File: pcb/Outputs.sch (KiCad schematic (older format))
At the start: 44 parts, among them P66 IG2, P67 IG1, P81 IG3, P82 IG4, P84 Ignitor2, P85 Ignitor1, P86 Ignitor3, P87 Ignitor4, Q10 VNN7NV0413TR, Q11 VNN7NV0413TR, Q9 VNN7NV0413TR, U12 TC442XA, U9 TC442XA

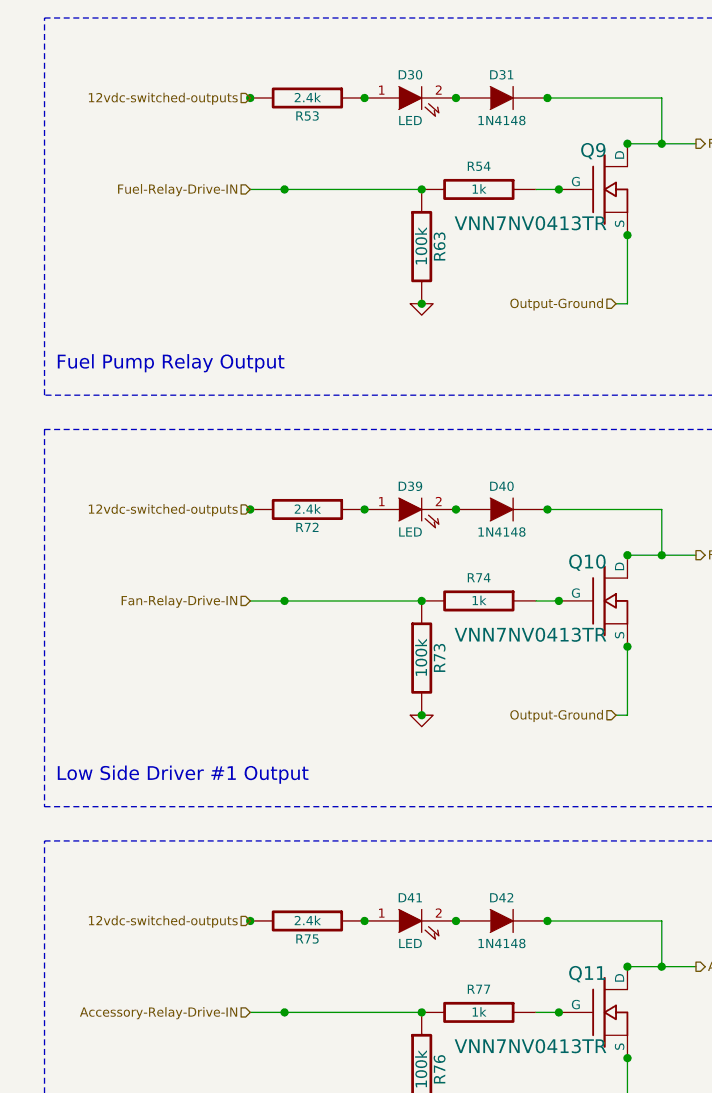
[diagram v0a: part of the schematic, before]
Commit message: Changed 2.4k ohm resistor to 2.43k ohm resistor due to physical size issue.
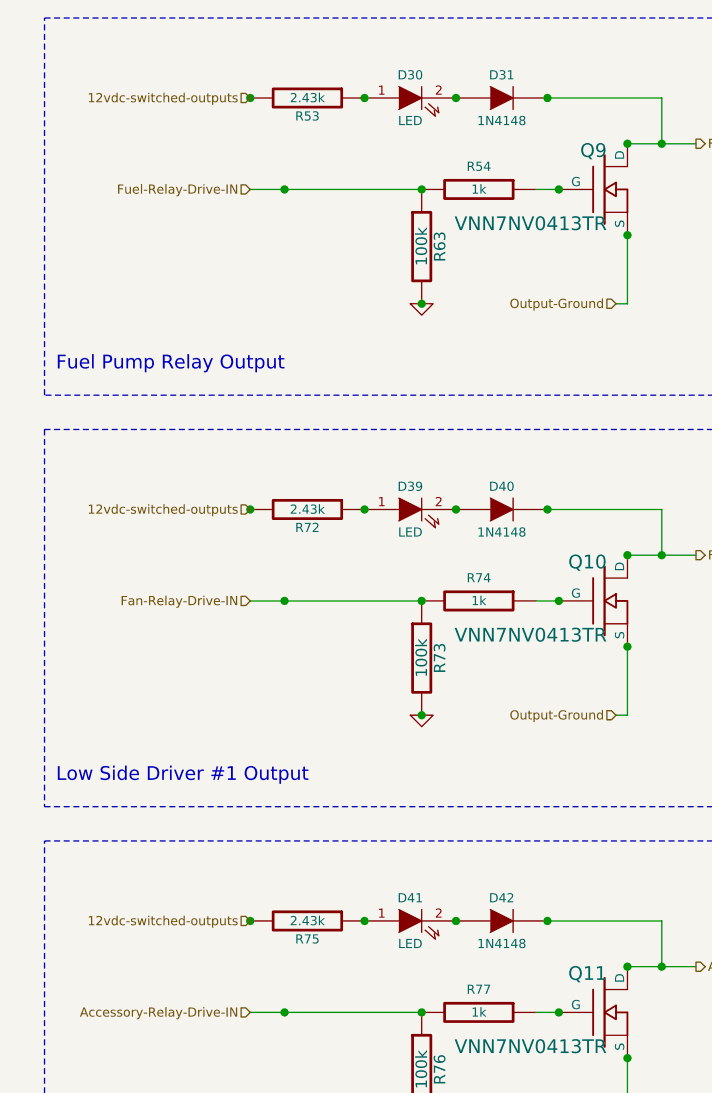
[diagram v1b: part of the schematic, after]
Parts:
- R53, R72, R75: value 2.4k -> 2.43k

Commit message: Added LEDs and resistors to ignitor outputs.
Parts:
- removed D31: 1N4148, symbol DIODE
- removed Q9: VNN7NV0413TR, symbol MOSFET_N
- added D? (x4): LED, symbol LED
- added R?: 1k, symbol R
- added R? (x4): 2.4k, symbol R
- added U?: VN5E160AS-E, symbol VN5E160AS-E
- R?: renamed from R53; value 2.43k -> 2.4k
- R?: renamed from R72; value 2.43k -> 2.4k
- R?: renamed from R75; value 2.43k -> 2.4k
- R?: renamed from R91; value 160 -> 100
- R?: renamed from R92; value 160 -> 100
- R?: renamed from R101; value 160 -> 100
- R?: renamed from R100; value 160 -> 100
- renumbered C52 to C?, C57 to C?, D30 to D?, D40 to D?, D39 to D?, D41 to D?, D42 to D?, JP1 to JP?, JP2 to JP?, P66 to P?, P67 to P?, P82 to P?, P81 to P?, P85 to P?, P84 to P?, P87 to P?, P86 to P?, Q10 to Q?, Q11 to Q?, R54 to R?, R63 to R?, R73 to R?, R74 to R?, R77 to R?, R76 to R?, R90 to R?, R89 to R?, R88 to R?, R87 to R?, R104 to R?, R105 to R?, R102 to R?, R103 to R?, U9 to U?, U12 to U?
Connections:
- net labels added: 5vdc-analog, LSD1-IN, LSD1_Relay, PCB-GND
- net labels removed: 5vdc-cpu, Accessory-Relay-Drive-IN, Accessory_Relay
- wire segments 55 -> 62
- no-connect marks 4 -> 5
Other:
- note added: "Fuel Pump Relay High Side Driver Output"
- note added: "JP11 selects either\n5v or 12v \nDriver IC Supply"
- note added: "JPxx selects either\n5v or 12v \nDriver IC Supply"
- note added: "Radiator Cooling Fan Low Side Driver Output"
- note removed: "Fuel Pump Relay Output"
- note removed: "JP1 selects either\n5v or 12v \nDriver IC Supply"
- note removed: "JP2 selects either\n5v or 12v \nDriver IC Supply"
- note removed: "Low Side Driver #2 Output"
- note removed: "\nTC4426A has two inverting drivers, \nwhile the TC4427A has two non-inverting drivers, \nThe TC4428A has one inverting and one non-inverting driver."
- moved on the sheet: C?, D?, JP?, R?

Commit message: Changed fuel pump LSD out for high side driver, removed Fan and LSD1 individual low side drivers for a pair of dual MOSFET low side drivers.
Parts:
- removed D?: LED, symbol LED
- removed D?: 1N4148, symbol DIODE
- removed Q? (x2): VNN7NV0413TR, symbol MOSFET_N
- removed R?: 1k, symbol R
- removed R?: 2.4k, symbol R
- removed R?: 100k, symbol R
- added D? (x3): LED, symbol LED
- added D? (x3): 1N4148, symbol DIODE
- added R? (x3): 1k, symbol R
- added R? (x3): 100k, symbol R
- added R? (x3): 2.4k, symbol R
- added U?, U??: VNS3NV04D, ~, symbol VNS3NV04D
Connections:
- net labels added: LSD1, LSD2, LSD2-IN, LSD3, LSD3-IN
- net labels removed: LSD1_Relay
- wire segments 62 -> 91
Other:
- moved on the sheet: D?, R?

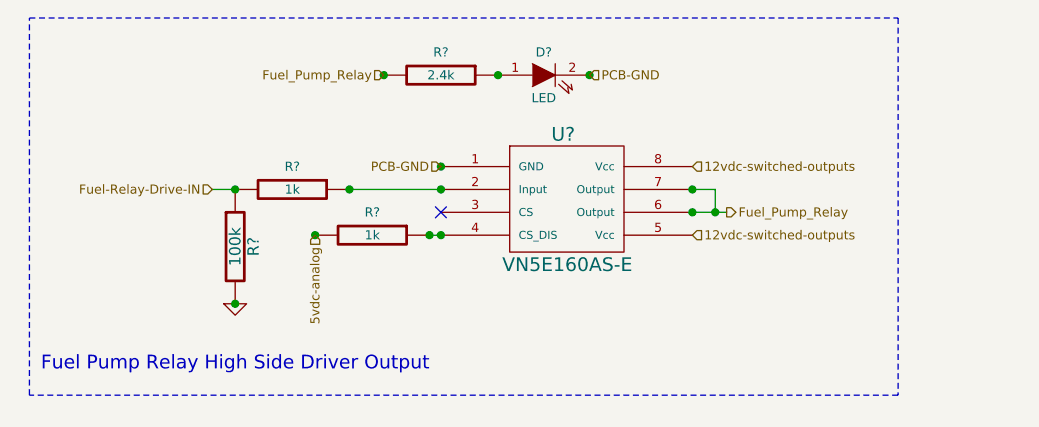
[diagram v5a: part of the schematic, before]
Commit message: Removed direct connection between Port A7 and the Fuel Pump HSD and added connection points to solder a jumper wire to select fuel pump HSD or LSD circuit.
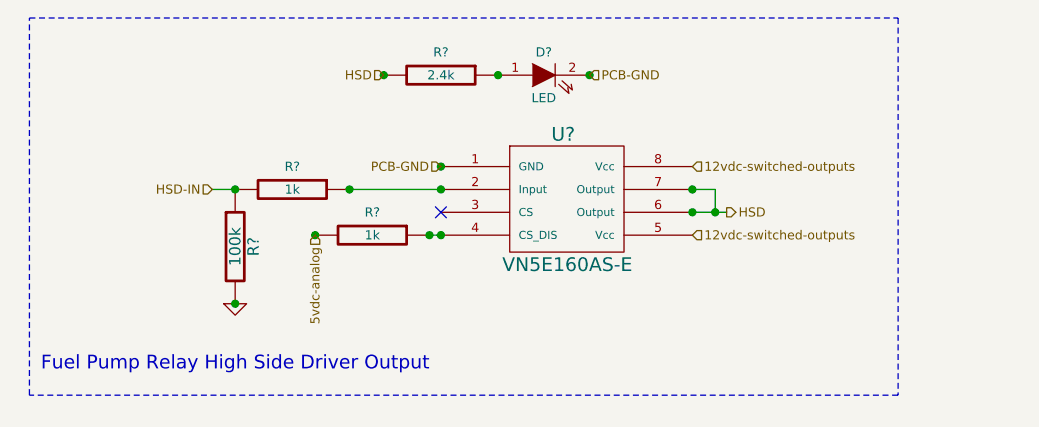
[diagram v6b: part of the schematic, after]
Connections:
- net labels added: HSD, HSD-IN
- net labels removed: Fuel-Relay-Drive-IN, Fuel_Pump_Relay
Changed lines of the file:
@@
 $EndComp
 Text HLabel 1450 1350 0    40   Input ~ 0
-Fuel-Relay-Drive-IN
-Text HLabel 2200 850  0    40   Input ~ 0
-Fuel_Pump_Relay
+HSD-IN
 $Comp
 L R R?
@@
 12vdc-switched-outputs
 Text HLabel 3700 1450 2    40   Output ~ 0
-Fuel_Pump_Relay
+HSD
 Wire Wire Line
 	3550 1450 3650 1450
@@
 	4250 5150 4250 5350
 Connection ~ 4250 5350
+Text HLabel 2200 850  0    40   Input ~ 0
+HSD
 $EndSCHEMATC

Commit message: Changed revision to 0.7-alpha and git hash to xxxxxxxxxx to show that this is in progress.
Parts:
- removed D? (x4): 1N4148, symbol DIODE
- removed D? (x7): LED, symbol LED
- removed R? (x4): 1k, symbol R
- removed R? (x7): 2.4k, symbol R
- removed R? (x3): 100k, symbol R
- removed U?: VN5E160AS-E, symbol VN5E160AS-E
- removed U?, U??: VNS3NV04D, ~, symbol VNS3NV04D
- added D40, D42, D? (x2): 1N4148, symbol DIODE
- added D41, D? (x4): LED, symbol LED
- added R75, R? (x4): 2.4k, symbol R
- added R76, R? (x2): 100k, symbol R
- added R77, R? (x3): 1k, symbol R
- added U??: VN5E160AS-E, ~, symbol VN5E160AS-E
- added U?? (x2): VNS3NV04D, ~, symbol VNS3NV04D
- R100, R101, R91, R92: renamed from R?; value 100 -> 160
- gave numbers to parts that had none: 30
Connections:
- net labels added: 5vdc-cpu, Fan-IN
- net labels removed: 5vdc-analog, Fan-Relay-Drive-IN
- wire segments 91 -> 78
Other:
- note added: "Fuel Pump Relay Output"
- note added: "JP1 selects either\n5v or 12v \nDriver IC Supply"
- note added: "JP2 selects either\n5v or 12v \nDriver IC Supply"
- note added: "Low Side Driver #2 and #3 Outputs"
- note added: "Radiator Fan and Low Side Driver #1 Outputs"
- note added: "\nTC4426A has two inverting drivers, \nwhile the TC4427A has two non-inverting drivers, \nThe TC4428A has one inverting and one non-inverting driver."
- note removed: "Fuel Pump Relay High Side Driver Output"
- note removed: "JP11 selects either\n5v or 12v \nDriver IC Supply"
- note removed: "JPxx selects either\n5v or 12v \nDriver IC Supply"
- note removed: "Low Side Driver #1 Output"
- note removed: "Radiator Cooling Fan Low Side Driver Output"
- moved on the sheet: C52, C57, D30, D39, JP1, JP2, R53, R54, R63, R72, R73, R74

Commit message: Started laying out PCB changes for SO-8 high side driver and new SO-8 low side drivers.
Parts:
- gave numbers to parts that had none: 18
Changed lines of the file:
@@
 Sheet 5 7
 Title "Jaguar PCB for FreeEMS"
-Date "5 feb 2014"
+Date "4 mar 2014"
 Rev "0.7-alpha"
 Comp "Git: xxxxxxxxxx"
@@
 Connection ~ 1200 1850
 Connection ~ 3200 850
-Connection ~ 1550 950
 Connection ~ 3600 850
 Wire Notes Line
@@
 $EndComp
 $Comp
-L GND #PWR029
+L GND #PWR40
 U 1 1 509C8648
 P 7700 4100
-F 0 "#PWR029" H 7700 4100 30  0001 C CNN
+F 0 "#PWR40" H 7700 4100 30  0001 C CNN
 F 1 "GND" H 7700 4030 30  0001 C CNN
 F 2 "" H 7700 4100 60  0001 C CNN
@@
 $EndComp
 $Comp
-L GND #PWR030
+L GND #PWR36
 U 1 1 509C8647
 P 7550 2900
-F 0 "#PWR030" H 7550 2900 30  0001 C CNN
+F 0 "#PWR36" H 7550 2900 30  0001 C CNN
 F 1 "GND" H 7550 2830 30  0001 C CNN
 F 2 "" H 7550 2900 60  0001 C CNN
@@
 $EndComp
 $Comp
-L GND #PWR031
+L GND #PWR39
 U 1 1 509C8646
 P 7700 3450
-F 0 "#PWR031" H 7700 3450 30  0001 C CNN
+F 0 "#PWR39" H 7700 3450 30  0001 C CNN
 F 1 "GND" H 7700 3380 30  0001 C CNN
 F 2 "" H 7700 3450 60  0001 C CNN
@@
 $EndComp
 $Comp
-L GND #PWR032
+L GND #PWR44
 U 1 1 509C8641
 P 9800 3900
-F 0 "#PWR032" H 9800 3900 30  0001 C CNN
+F 0 "#PWR44" H 9800 3900 30  0001 C CNN
 F 1 "GND" H 9800 3830 30  0001 C CNN
 F 2 "" H 9800 3900 60  0001 C CNN
@@
 JP1 selects either\n5v or 12v \nDriver IC Supply
 $Comp
-L GND #PWR033
+L GND #PWR43
 U 1 1 5092C12A
 P 9800 1950
-F 0 "#PWR033" H 9800 1950 30  0001 C CNN
+F 0 "#PWR43" H 9800 1950 30  0001 C CNN
 F 1 "GND" H 9800 1880 30  0001 C CNN
 F 2 "" H 9800 1950 60  0001 C CNN
@@
 $EndComp
 $Comp
-L GND #PWR034
+L GND #PWR37
 U 1 1 5092BF20
 P 7700 1500
-F 0 "#PWR034" H 7700 1500 30  0001 C CNN
+F 0 "#PWR37" H 7700 1500 30  0001 C CNN
 F 1 "GND" H 7700 1430 30  0001 C CNN
 F 2 "" H 7700 1500 60  0001 C CNN
@@
 $EndComp
 $Comp
-L GND #PWR035
+L GND #PWR35
 U 1 1 5092BF13
 P 7550 950
-F 0 "#PWR035" H 7550 950 30  0001 C CNN
+F 0 "#PWR35" H 7550 950 30  0001 C CNN
 F 1 "GND" H 7550 880 30  0001 C CNN
 F 2 "" H 7550 950 60  0001 C CNN
@@
 $EndComp
 $Comp
-L GND #PWR036
+L GND #PWR38
 U 1 1 5092BF09
 P 7700 2150
-F 0 "#PWR036" H 7700 2150 30  0001 C CNN
+F 0 "#PWR38" H 7700 2150 30  0001 C CNN
 F 1 "GND" H 7700 2080 30  0001 C CNN
 F 2 "" H 7700 2150 60  0001 C CNN
@@
 12vdc-switched-outputs
 $Comp
-L GND #PWR037
+L GND #PWR30
 U 1 1 4F2F3E3F
 P 1100 5500
-F 0 "#PWR037" H 1100 5500 30  0001 C CNN
+F 0 "#PWR30" H 1100 5500 30  0001 C CNN
 F 1 "GND" H 1100 5430 30  0001 C CNN
 F 2 "" H 1100 5500 60  0001 C CNN
@@
 $EndComp
 $Comp
-L GND #PWR038
+L GND #PWR29
 U 1 1 4F2F3E2D
 P 1100 3650
-F 0 "#PWR038" H 1100 3650 30  0001 C CNN
+F 0 "#PWR29" H 1100 3650 30  0001 C CNN
 F 1 "GND" H 1100 3580 30  0001 C CNN
 F 2 "" H 1100 3650 60  0001 C CNN
@@
 $EndComp
 $Comp
-L GND #PWR039
+L GND #PWR31
 U 1 1 4F2F3E0C
 P 1200 1850
-F 0 "#PWR039" H 1200 1850 30  0001 C CNN
+F 0 "#PWR31" H 1200 1850 30  0001 C CNN
 F 1 "GND" H 1200 1780 30  0001 C CNN
 F 2 "" H 1200 1850 60  0001 C CNN
@@
 $EndComp
 $Comp
-L VN5E160AS-E U??
+L VN5E160AS-E U5
 U 1 1 52F270CB
 P 2650 1400
-F 0 "U??" H 2635 1691 60  0000 C CNN
+F 0 "U5" H 2635 1691 60  0000 C CNN
 F 1 "VN5E160AS-E" H 2653 1121 60  0000 C CNN
 F 2 "~" H 2650 1400 60  0000 C CNN
@@
 $EndComp
 $Comp
-L VNS3NV04D U??
+L VNS3NV04D U10
 U 1 1 52F270DA
 P 3050 3200
-F 0 "U??" H 3035 3491 60  0000 C CNN
+F 0 "U10" H 3035 3491 60  0000 C CNN
 F 1 "VNS3NV04D" H 3053 2921 60  0000 C CNN
 F 2 "~" H 3050 3200 60  0000 C CNN
@@
 $EndComp
 $Comp
-L VNS3NV04D U??
+L VNS3NV04D U14
 U 1 1 52F270E9
 P 3050 5050
-F 0 "U??" H 3035 5341 60  0000 C CNN
+F 0 "U14" H 3035 5341 60  0000 C CNN
 F 1 "VNS3NV04D" H 3053 4771 60  0000 C CNN
 F 2 "~" H 3050 5050 60  0000 C CNN
@@
 Connection ~ 9050 900
 $Comp
-L LED D?
+L LED D50
 U 1 1 52F2735A
 P 8850 900
-F 0 "D?" H 8850 1000 40  0000 C CNN
+F 0 "D50" H 8850 1000 40  0000 C CNN
 F 1 "LED" H 8850 800 40  0000 C CNN
 F 2 "" H 8850 900 60  0001 C CNN
@@
 $EndComp
 $Comp
-L R R?
+L R R64
 U 1 1 52F27360
 P 9300 900
-F 0 "R?" V 9380 900 40  0000 C CNN
+F 0 "R64" V 9380 900 40  0000 C CNN
 F 1 "2.4k" V 9300 900 40  0000 C CNN
 F 2 "" H 9300 900 60  0001 C CNN
@@
 Connection ~ 9050 2100
 $Comp
-L LED D?
+L LED D51
 U 1 1 52F27367
 P 8850 2100
-F 0 "D?" H 8850 2200 40  0000 C CNN
+F 0 "D51" H 8850 2200 40  0000 C CNN
 F 1 "LED" H 8850 2000 40  0000 C CNN
 F 2 "" H 8850 2100 60  0001 C CNN
@@
 $EndComp
 $Comp
-L R R?
+L R R65
 U 1 1 52F2736D
 P 9300 2100
-F 0 "R?" V 9380 2100 40  0000 C CNN
+F 0 "R65" V 9380 2100 40  0000 C CNN
 F 1 "2.4k" V 9300 2100 40  0000 C CNN
 F 2 "" H 9300 2100 60  0001 C CNN
@@
 	9550 1600 9500 1600
 $Comp
-L GND #PWR?
+L GND #PWR41
 U 1 1 52F274AB
 P 8650 950
-F 0 "#PWR?" H 8650 950 30  0001 C CNN
+F 0 "#PWR41" H 8650 950 30  0001 C CNN
 F 1 "GND" H 8650 880 30  0001 C CNN
 F 2 "" H 8650 950 60  0001 C CNN
@@
 $EndComp
 $Comp
-L GND #PWR?
+L GND #PWR42
 U 1 1 52F274B1
 P 8650 2150
-F 0 "#PWR?" H 8650 2150 30  0001 C CNN
+F 0 "#PWR42" H 8650 2150 30  0001 C CNN
 F 1 "GND" H 8650 2080 30  0001 C CNN
 F 2 "" H 8650 2150 60  0001 C CNN
@@
 12vdc-switched-outputs
 $Comp
-L R R?
+L R R62
 U 1 1 52F2813A
 P 3050 3750
-F 0 "R?" V 3130 3750 40  0000 C CNN
+F 0 "R62" V 3130 3750 40  0000 C CNN
 F 1 "2.4k" V 3050 3750 40  0000 C CNN
 F 2 "" H 3050 3750 60  0001 C CNN
@@
 $EndComp
 $Comp
-L LED D?
+L LED D31
 U 1 1 52F28140
 P 3500 3750
-F 0 "D?" H 3500 3850 40  0000 C CNN
+F 0 "D31" H 3500 3850 40  0000 C CNN
 F 1 "LED" H 3500 3650 40  0000 C CNN
 F 2 "" H 3500 3750 60  0001 C CNN
@@
 Connection ~ 1650 3350
 $Comp
-L GND #PWR?
+L GND #PWR32
 U 1 1 52F28353
 P 1650 3850
-F 0 "#PWR?" H 1650 3850 30  0001 C CNN
+F 0 "#PWR32" H 1650 3850 30  0001 C CNN
 F 1 "GND" H 1650 3780 30  0001 C CNN
 F 2 "" H 1650 3850 60  0001 C CNN
@@
 $EndComp
 $Comp
-L R R?
+L R R59
 U 1 1 52F28359
 P 1900 3350
-F 0 "R?" V 2000 3350 40  0000 C CNN
+F 0 "R59" V 2000 3350 40  0000 C CNN
 F 1 "1k" V 1900 3350 40  0000 C CNN
 F 2 "" H 1900 3350 60  0001 C CNN
@@
 LSD1-IN
 $Comp
-L R R?
+L R R14
 U 1 1 52F28360
 P 1650 3600
-F 0 "R?" V 1730 3600 50  0000 C CNN
+F 0 "R14" V 1730 3600 50  0000 C CNN
 F 1 "100k" V 1650 3600 50  0000 C CNN
 F 2 "" H 1650 3600 60  0001 C CNN
@@
 Connection ~ 4100 3750
 $Comp
-L DIODE D?
+L DIODE D49
 U 1 1 52F28146
 P 3900 3750
-F 0 "D?" H 3900 3850 40  0000 C CNN
+F 0 "D49" H 3900 3850 40  0000 C CNN
 F 1 "1N4148" H 3900 3650 40  0000 C CNN
 F 2 "" H 3900 3750 60  0001 C CNN
@@
 PCB-GND
 $Comp
-L GND #PWR?
+L GND #PWR34
 U 1 1 52F2881A
 P 3200 900
-F 0 "#PWR?" H 3200 900 30  0001 C CNN
+F 0 "#PWR34" H 3200 900 30  0001 C CNN
 F 1 "GND" H 3200 830 30  0001 C CNN
 F 2 "" H 3200 900 60  0001 C CNN
@@
 NoConn ~ 2100 1450
 $Comp
-L R R?
+L R R56
 U 1 1 52F288C8
 P 1850 1550
-F 0 "R?" V 1750 1550 40  0000 C CNN
+F 0 "R56" V 1750 1550 40  0000 C CNN
 F 1 "1k" V 1850 1550 40  0000 C CNN
 F 2 "" H 1850 1550 60  0001 C CNN
@@
 Connection ~ 1650 5200
 $Comp
-L GND #PWR?
+L GND #PWR33
 U 1 1 52F26A48
 P 1650 5700
-F 0 "#PWR?" H 1650 5700 30  0001 C CNN
+F 0 "#PWR33" H 1650 5700 30  0001 C CNN
 F 1 "GND" H 1650 5630 30  0001 C CNN
 F 2 "" H 1650 5700 60  0001 C CNN
@@
 $EndComp
 $Comp
-L R R?
+L R R60
 U 1 1 52F26A4E
 P 1900 5200
-F 0 "R?" V 2000 5200 40  0000 C CNN
+F 0 "R60" V 2000 5200 40  0000 C CNN
 F 1 "1k" V 1900 5200 40  0000 C CNN
 F 2 "" H 1900 5200 60  0001 C CNN
@@
 LSD3-IN
 $Comp
-L R R?
+L R R15
 U 1 1 52F26A55
 P 1650 5450
-F 0 "R?" V 1730 5450 50  0000 C CNN
+F 0 "R15" V 1730 5450 50  0000 C CNN
 F 1 "100k" V 1650 5450 50  0000 C CNN
 F 2 "" H 1650 5450 60  0001 C CNN
@@
 12vdc-switched-outputs
 $Comp
-L R R?
+L R R61
 U 1 1 52F27903
 P 3000 5600
-F 0 "R?" V 3080 5600 40  0000 C CNN
+F 0 "R61" V 3080 5600 40  0000 C CNN
 F 1 "2.4k" V 3000 5600 40  0000 C CNN
 F 2 "" H 3000 5600 60  0001 C CNN
@@
 $EndComp
 $Comp
-L LED D?
+L LED D3
 U 1 1 52F27909
 P 3450 5600
-F 0 "D?" H 3450 5700 40  0000 C CNN
+F 0 "D3" H 3450 5700 40  0000 C CNN
 F 1 "LED" H 3450 5500 40  0000 C CNN
 F 2 "" H 3450 5600 60  0001 C CNN
@@
 Connection ~ 4050 5600
 $Comp
-L DIODE D?
+L DIODE D32
 U 1 1 52F27911
 P 3850 5600
-F 0 "D?" H 3850 5700 40  0000 C CNN
+F 0 "D32" H 3850 5700 40  0000 C CNN
 F 1 "1N4148" H 3850 5500 40  0000 C CNN
 F 2 "" H 3850 5600 60  0001 C CNN
